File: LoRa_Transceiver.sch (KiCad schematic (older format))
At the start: 10 parts, among them J10 Conn_01x02_Male, J11 Conn_01x02_Male, J12 Conn_01x02_Male, J13 Conn_01x02_Male, J7 SMA Female, J8 Conn_01x02_Male, J9 Conn_01x02_Male, U1 RFM95W-868S2

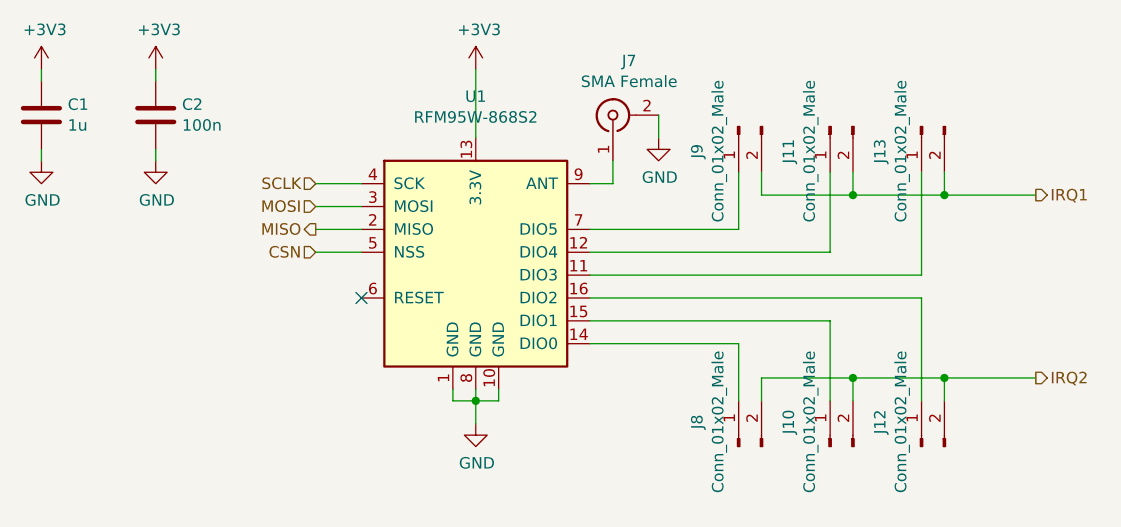
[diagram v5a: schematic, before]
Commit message: Add connector for external chamber connection and change SMA to U.FL connector
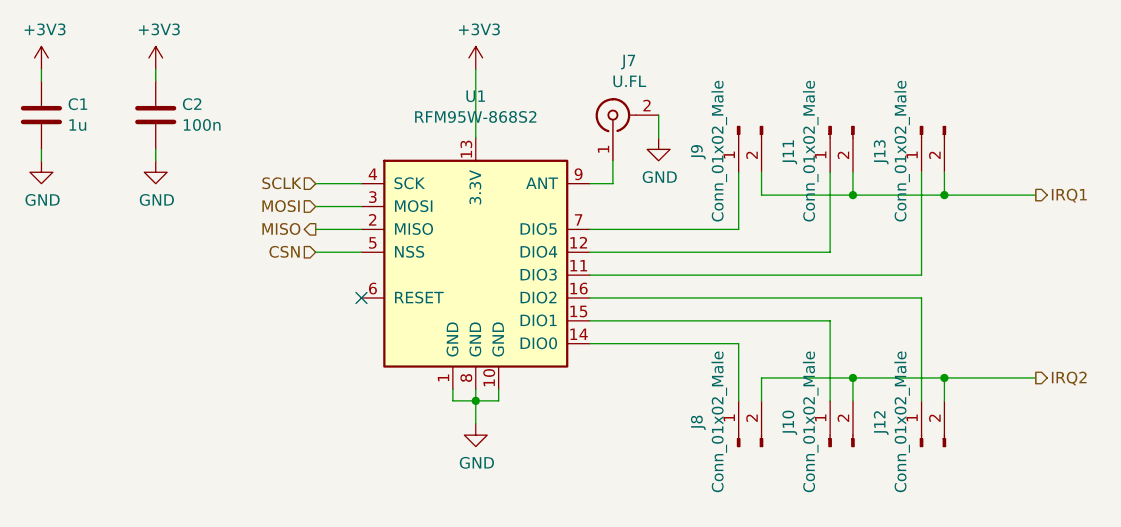
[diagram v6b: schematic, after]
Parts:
- J7: value SMA Female -> U.FL; footprint co2_sensor_node:TE_5-1814832-2_C482015 -> Connector_Coaxial:U.FL_Hirose_U.FL-R-SMT-1_Vertical; LCSC C482015 -> C88374
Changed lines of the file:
@@
 P 5000 3300
 F 0 "J7" V 5237 3229 50  0000 C CNN
-F 1 "SMA Female" V 5146 3229 50  0000 C CNN
-F 2 "co2_sensor_node:TE_5-1814832-2_C482015" H 5000 3300 50  0001 C CNN
-F 3 " ~" H 5000 3300 50  0001 C CNN
-F 4 "C482015" H 5000 3300 50  0001 C CNN "LCSC"
+F 1 "U.FL" V 5146 3229 50  0000 C CNN
+F 2 "Connector_Coaxial:U.FL_Hirose_U.FL-R-SMT-1_Vertical" H 5000 3300 50  0001 C CNN
+F 3 "https://datasheet.lcsc.com/szlcsc/1811091710_HRS-Hirose-U-FL-R-SMT-1-80_C88374.pdf" H 5000 3300 50  0001 C CNN
+F 4 "C88374" H 5000 3300 50  0001 C CNN "LCSC"
 	1    5000 3300
 	0    -1   -1   0
